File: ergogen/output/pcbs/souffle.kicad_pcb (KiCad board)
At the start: 2 copper layers, 130.3 x 93.2 mm, 162 parts

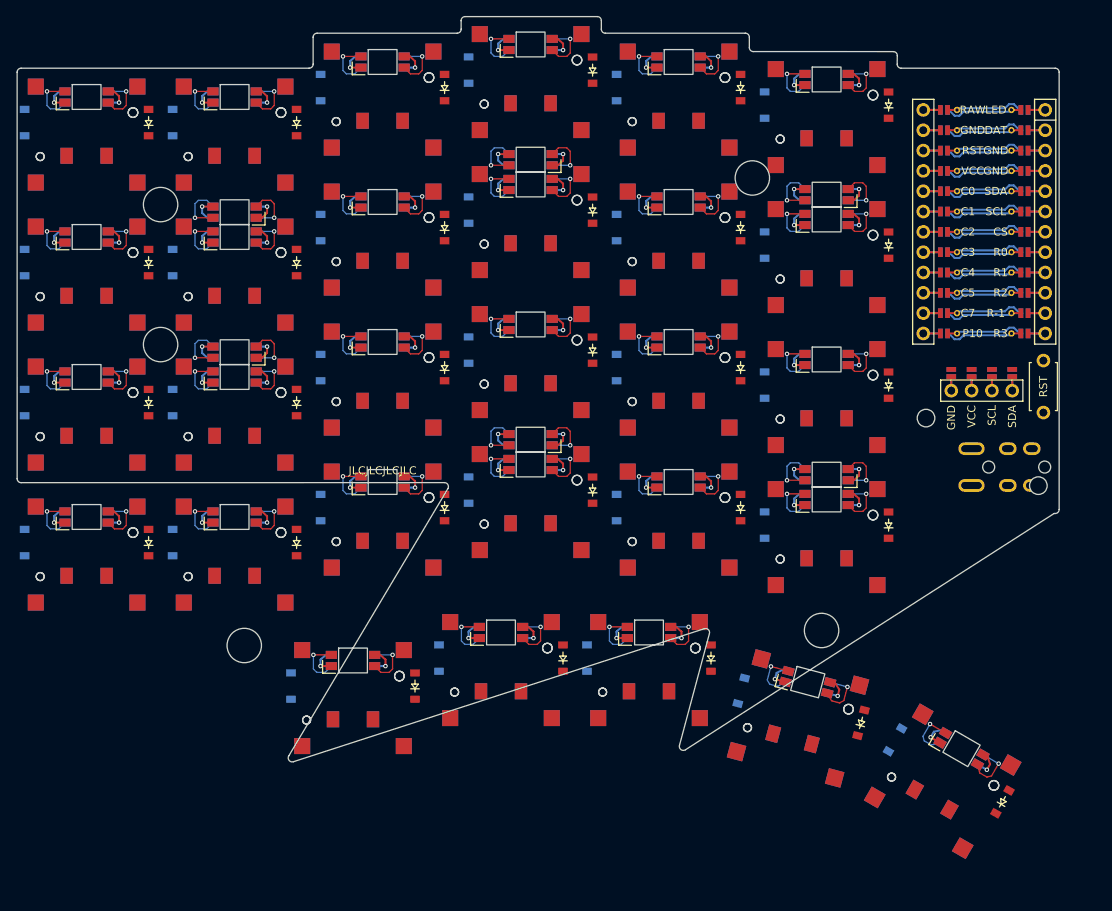
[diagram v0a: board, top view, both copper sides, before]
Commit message: fix: number row on top and improved outline
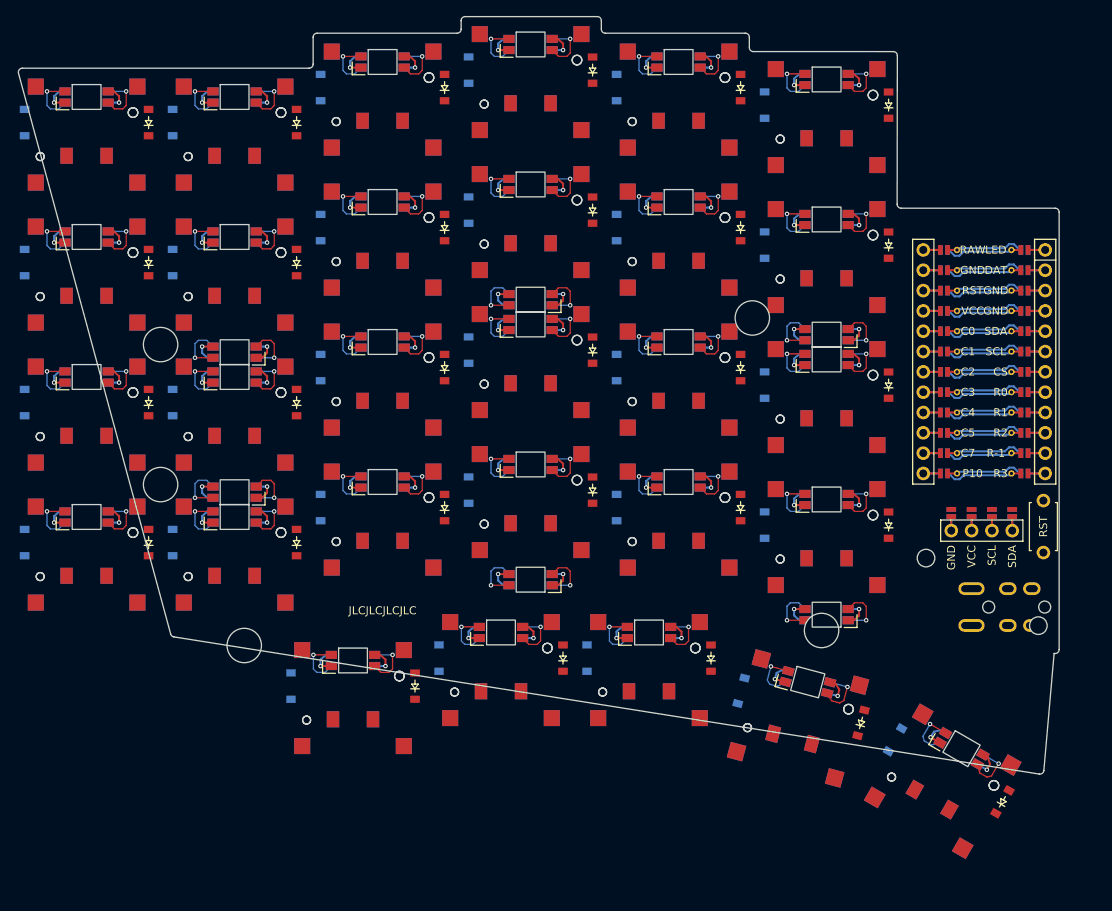
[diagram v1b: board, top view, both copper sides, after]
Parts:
- moved MCU1 17.5 mm to (212.2, 74.6)
- moved MH5 17.5 mm to (183.2, 70.4)
- moved LED30 17.5 mm to (192.5, 72.5)
- moved LED31 17.5 mm to (155.5, 68.1)
- moved LED32 17.5 mm to (118.5, 74.7)
- moved LED33 17.5 mm to (118.5, 92.2)
- moved LED34 17.5 mm to (155.5, 103.1)
- moved LED35 17.5 mm to (192.5, 107.5)
- moved MH1 17.5 mm to (204.9, 100.4)
- moved MH2 17.5 mm to (219.0, 108.9)
- moved MH3 17.5 mm to (109.2, 73.8)
- moved MH4 17.5 mm to (109.2, 91.2)
- moved RST1 17.5 mm to (219.6, 96.5)
- moved TRRS1 17.5 mm to (221.4, 106.6)
- moved DISP1 17.5 mm to (211.9, 80.3)
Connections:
- D1 pad 1: R-1 -> R2
- D1 pad 2: outer_number_B -> outer_bottom_B
- D10 pad 1: R2 -> R1
- D10 pad 2: ring_bottom_B -> ring_home_B
- D11 pad 1: R1 -> R0
- D11 pad 2: ring_home_B -> ring_top_B
- D12 pad 1: R0 -> R4
- D12 pad 2: ring_top_B -> ring_number_B
- D13 pad 1: R-1 -> R2
- D13 pad 2: middle_number_B -> middle_bottom_B
- D14 pad 1: R2 -> R1
- D14 pad 2: middle_bottom_B -> middle_home_B
- D15 pad 1: R1 -> R0
- D15 pad 2: middle_home_B -> middle_top_B
- D16 pad 1: R0 -> R4
- D16 pad 2: middle_top_B -> middle_number_B
- D17 pad 1: R-1 -> R2
- D17 pad 2: index_number_B -> index_bottom_B
- D18 pad 1: R2 -> R1
- D18 pad 2: index_bottom_B -> index_home_B
- D19 pad 1: R1 -> R0
- D19 pad 2: index_home_B -> index_top_B
- D2 pad 1: R2 -> R1
- D2 pad 2: outer_bottom_B -> outer_home_B
- D20 pad 1: R0 -> R4
- D20 pad 2: index_top_B -> index_number_B
- D21 pad 1: R-1 -> R2
- D21 pad 2: inner_number_B -> inner_bottom_B
- D22 pad 1: R2 -> R1
- D22 pad 2: inner_bottom_B -> inner_home_B
- D23 pad 1: R1 -> R0
- D23 pad 2: inner_home_B -> inner_top_B
- D24 pad 1: R0 -> R4
- D24 pad 2: inner_top_B -> inner_number_B
- D3 pad 1: R1 -> R0
- D3 pad 2: outer_home_B -> outer_top_B
- D30 pad 1: R-1 -> R2
- D30 pad 2: outer_number_F -> outer_bottom_F
- D31 pad 1: R2 -> R1
- D31 pad 2: outer_bottom_F -> outer_home_F
- D32 pad 1: R1 -> R0
- D32 pad 2: outer_home_F -> outer_top_F
- D33 pad 1: R0 -> R4
- D33 pad 2: outer_top_F -> outer_number_F
- D34 pad 1: R-1 -> R2
- D34 pad 2: pinky_number_F -> pinky_bottom_F
- D35 pad 1: R2 -> R1
- D35 pad 2: pinky_bottom_F -> pinky_home_F
- D36 pad 1: R1 -> R0
- D36 pad 2: pinky_home_F -> pinky_top_F
- D37 pad 1: R0 -> R4
- D37 pad 2: pinky_top_F -> pinky_number_F
- D38 pad 1: R-1 -> R2
- D38 pad 2: ring_number_F -> ring_bottom_F
- D39 pad 1: R2 -> R1
- D39 pad 2: ring_bottom_F -> ring_home_F
- D4 pad 1: R0 -> R4
- D4 pad 2: outer_top_B -> outer_number_B
- D40 pad 1: R1 -> R0
- D40 pad 2: ring_home_F -> ring_top_F
- D41 pad 1: R0 -> R4
- D41 pad 2: ring_top_F -> ring_number_F
- D42 pad 1: R-1 -> R2
- D42 pad 2: middle_number_F -> middle_bottom_F
- D43 pad 1: R2 -> R1
- D43 pad 2: middle_bottom_F -> middle_home_F
- D44 pad 1: R1 -> R0
- D44 pad 2: middle_home_F -> middle_top_F
- D45 pad 1: R0 -> R4
- D45 pad 2: middle_top_F -> middle_number_F
- D46 pad 1: R-1 -> R2
- D46 pad 2: index_number_F -> index_bottom_F
- D47 pad 1: R2 -> R1
- D47 pad 2: index_bottom_F -> index_home_F
- D48 pad 1: R1 -> R0
- D48 pad 2: index_home_F -> index_top_F
- D49 pad 1: R0 -> R4
- D49 pad 2: index_top_F -> index_number_F
- D5 pad 1: R-1 -> R2
- D5 pad 2: pinky_number_B -> pinky_bottom_B
- D50 pad 1: R-1 -> R2
- D50 pad 2: inner_number_F -> inner_bottom_F
- D51 pad 1: R2 -> R1
- D51 pad 2: inner_bottom_F -> inner_home_F
- D52 pad 1: R1 -> R0
- D52 pad 2: inner_home_F -> inner_top_F
- D53 pad 1: R0 -> R4
- D53 pad 2: inner_top_F -> inner_number_F
- D6 pad 1: R2 -> R1
- D6 pad 2: pinky_bottom_B -> pinky_home_B
- D7 pad 1: R1 -> R0
- D7 pad 2: pinky_home_B -> pinky_top_B
- D8 pad 1: R0 -> R4
- D8 pad 2: pinky_top_B -> pinky_number_B
- D9 pad 1: R-1 -> R2
- D9 pad 2: ring_number_B -> ring_bottom_B
- LED1 pad 2: LED_18 -> LED_21
- LED1 pad 4: LED_19 -> LED_20
- LED10 pad 2: LED_15 -> LED_14
- LED10 pad 4: LED_14 -> LED_13
- LED11 pad 2: LED_14 -> LED_13
- LED11 pad 4: LED_13 -> LED_12
- LED12 pad 2: LED_13 -> LED_12
- LED12 pad 4: LED_12 -> LED_13
- LED13 pad 2: LED_11 -> LED_10
- LED13 pad 4: LED_12 -> LED_9
- LED14 pad 2: LED_10 -> LED_11
- LED14 pad 4: LED_9 -> LED_10
- LED15 pad 2: LED_11 -> LED_12
- LED15 pad 4: LED_10 -> LED_11
- LED16 pad 2: LED_12 -> LED_11
- LED16 pad 4: LED_11 -> LED_12
- LED17 pad 2: LED_4 -> LED_7
- LED17 pad 4: LED_5 -> LED_6
- LED18 pad 2: LED_7 -> LED_6
- LED18 pad 4: LED_6 -> LED_5
- LED19 pad 2: LED_6 -> LED_5
- LED19 pad 4: LED_5 -> LED_4
- LED2 pad 2: LED_21 -> LED_20
- LED2 pad 4: LED_20 -> LED_19
- LED20 pad 2: LED_5 -> LED_4
- LED20 pad 4: LED_4 -> LED_5
- LED21 pad 2: LED_3 -> LED_2
- LED21 pad 4: LED_4 -> LED_1
- LED22 pad 2: LED_2 -> LED_3
- LED22 pad 4: LED_1 -> LED_2
- LED23 pad 2: LED_3 -> LED_4
- LED23 pad 4: LED_2 -> LED_3
- LED24 pad 2: LED_4 -> LED_3
- LED24 pad 4: LED_3 -> LED_4
- LED3 pad 2: LED_20 -> LED_19
- LED3 pad 4: LED_19 -> LED_18
- LED4 pad 2: LED_19 -> LED_18
- LED4 pad 4: LED_18 -> LED_19
- LED5 pad 2: LED_17 -> LED_16
- LED5 pad 4: LED_16 -> LED_15
- LED6 pad 2: LED_16 -> LED_17
- LED6 pad 4: LED_15 -> LED_16
- LED7 pad 2: LED_17 -> LED_18
- LED7 pad 4: LED_16 -> LED_17
- LED8 pad 2: LED_18 -> LED_17
- LED8 pad 4: LED_17 -> LED_16
- LED9 pad 2: LED_12 -> LED_15
- LED9 pad 4: LED_13 -> LED_14
- S1 pad 1: outer_number_B -> outer_bottom_B
- S10 pad 1: ring_bottom_B -> ring_home_B
- S11 pad 1: ring_home_B -> ring_top_B
- S12 pad 1: ring_top_B -> ring_number_B
- S13 pad 1: middle_number_B -> middle_bottom_B
- S14 pad 1: middle_bottom_B -> middle_home_B
- S15 pad 1: middle_home_B -> middle_top_B
- S16 pad 1: middle_top_B -> middle_number_B
- S17 pad 1: index_number_B -> index_bottom_B
- S18 pad 1: index_bottom_B -> index_home_B
- S19 pad 1: index_home_B -> index_top_B
- S2 pad 1: outer_bottom_B -> outer_home_B
- S20 pad 1: index_top_B -> index_number_B
- S21 pad 1: inner_number_B -> inner_bottom_B
- S22 pad 1: inner_bottom_B -> inner_home_B
- S23 pad 1: inner_home_B -> inner_top_B
- S24 pad 1: inner_top_B -> inner_number_B
- S3 pad 1: outer_home_B -> outer_top_B
- S30 pad 1: outer_number_F -> outer_bottom_F
- S31 pad 1: outer_bottom_F -> outer_home_F
- S32 pad 1: outer_home_F -> outer_top_F
- S33 pad 1: outer_top_F -> outer_number_F
- S34 pad 1: pinky_number_F -> pinky_bottom_F
- S35 pad 1: pinky_bottom_F -> pinky_home_F
- S36 pad 1: pinky_home_F -> pinky_top_F
- S37 pad 1: pinky_top_F -> pinky_number_F
- S38 pad 1: ring_number_F -> ring_bottom_F
- S39 pad 1: ring_bottom_F -> ring_home_F
- S4 pad 1: outer_top_B -> outer_number_B
- S40 pad 1: ring_home_F -> ring_top_F
- S41 pad 1: ring_top_F -> ring_number_F
- S42 pad 1: middle_number_F -> middle_bottom_F
- S43 pad 1: middle_bottom_F -> middle_home_F
- S44 pad 1: middle_home_F -> middle_top_F
- S45 pad 1: middle_top_F -> middle_number_F
- S46 pad 1: index_number_F -> index_bottom_F
- S47 pad 1: index_bottom_F -> index_home_F
- S48 pad 1: index_home_F -> index_top_F
- S49 pad 1: index_top_F -> index_number_F
- S5 pad 1: pinky_number_B -> pinky_bottom_B
- S50 pad 1: inner_number_F -> inner_bottom_F
- S51 pad 1: inner_bottom_F -> inner_home_F
- S52 pad 1: inner_home_F -> inner_top_F
- S53 pad 1: inner_top_F -> inner_number_F
- S6 pad 1: pinky_bottom_B -> pinky_home_B
- S7 pad 1: pinky_home_B -> pinky_top_B
- S8 pad 1: pinky_top_B -> pinky_number_B
- S9 pad 1: ring_number_B -> ring_bottom_B
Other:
- board size 130.3 x 93.2 mm -> 130.1 x 94.7 mm

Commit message: feat: outline improvements
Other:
- board size 130.1 x 94.7 mm -> 134.9 x 109.8 mm
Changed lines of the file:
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@@
   (segment (start 197.45 106.4525) (end 197.45 108.2125) (width 0.15) (layer "F.Cu") (net 143))
   (segment (start 197.029 106.0275) (end 197.45 106.4525) (width 0.15) (layer "F.Cu") (net 143))
-  (gr_line (start 110.50826649856596 109.92527651860325) (end 91.48622889852672 39.83343914341975) (layer Edge.Cuts) (stroke (width 0.15) (type default)))
-(gr_line (start 91.9687610950968 39.202482330781216) (end 127.8150135 39.201513513148655) (layer Edge.Cuts) (stroke (width 0.15) (type default)))
+  (gr_line (start 91.2502786953727 111.93679999635788) (end 91.31455549192064 39.702041598866344) (layer Edge.Cuts) (stroke (width 0.15) (type default)))
+(gr_line (start 91.81454179192065 39.202486498870485) (end 127.8150135 39.20151351314865) (layer Edge.Cuts) (stroke (width 0.15) (type default)))
 (gr_line (start 128.315 38.701513513148655) (end 128.315 35.3275) (layer Edge.Cuts) (stroke (width 0.15) (type default)))
 (gr_line (start 128.815 34.8275) (end 146.315 34.8275) (layer Edge.Cuts) (stroke (width 0.15) (type default)))
@@
 (gr_line (start 183.34287840000002 37.12312159204324) (end 200.8424827703032 37.12737825256575) (layer Edge.Cuts) (stroke (width 0.15) (type default)))
 (gr_line (start 201.34236077036712 37.628016802540515) (end 201.31863938512134 56.201861450012075) (layer Edge.Cuts) (stroke (width 0.15) (type default)))
-(gr_line (start 220.93800000000002 112.3635) (end 219.65752596395185 126.98539423067496) (layer Edge.Cuts) (stroke (width 0.15) (type default)))
-(gr_line (start 219.08114720800037 127.43560839237159) (end 110.91252714391037 110.28815311369672) (layer Edge.Cuts) (stroke (width 0.15) (type default)))
+(gr_line (start 221.6070711821377 104.9663415844974) (end 226.0923281969262 115.6359149762103) (layer Edge.Cuts) (stroke (width 0.15) (type default)))
+(gr_line (start 226.0654764006069 116.07782689603465) (end 211.09156059668345 142.27125340028437) (layer Edge.Cuts) (stroke (width 0.15) (type default)))
+(gr_line (start 210.44136417514045 142.47398553796899) (end 176.60167485384602 126.25365946744344) (layer Edge.Cuts) (stroke (width 0.15) (type default)))
+(gr_line (start 176.4280428580794 126.20634746780448) (end 161.62301991140092 124.94372737349019) (layer Edge.Cuts) (stroke (width 0.15) (type default)))
+(gr_line (start 161.4782637171782 124.95248967103738) (end 144.8505883399894 128.42692930209176) (layer Edge.Cuts) (stroke (width 0.15) (type default)))
+(gr_line (start 144.74831955000005 128.4375) (end 124.6650889942857 128.4375) (layer Edge.Cuts) (stroke (width 0.15) (type default)))
+(gr_line (start 124.44649265438869 128.38718392921672) (end 91.53168215547566 112.38692882557845) (layer Edge.Cuts) (stroke (width 0.15) (type default)))
 (gr_line (start 201.81863898518517 56.7025) (end 221.068 56.7025) (layer Edge.Cuts) (stroke (width 0.15) (type default)))
-(gr_line (start 221.568 57.2025) (end 221.568 111.8635) (layer Edge.Cuts) (stroke (width 0.15) (type default)))
-(gr_line (start 221.068 112.3635) (end 220.93800000000002 112.3635) (layer Edge.Cuts) (stroke (width 0.15) (type default)))
-(gr_arc (start 91.9687610950968 39.20248233078121) (mid 91.5716065950968 39.39874303078121) (end 91.48622889509679 39.83343913078121) (layer Edge.Cuts) (stroke (width 0.15) (type default)))
+(gr_line (start 221.568 57.2025) (end 221.568 104.77257712698844) (layer Edge.Cuts) (stroke (width 0.15) (type default)))
+(gr_arc (start 91.81454179192065 39.202486498863436) (mid 91.46115449192064 39.348780598863435) (end 91.31455549192064 39.70204159886344) (layer Edge.Cuts) (stroke (width 0.15) (type default)))
 (gr_arc (start 127.81501349999999 39.201513513148655) (mid 128.1685582 39.05506211314866) (end 128.315 38.701513513148655) (layer Edge.Cuts) (stroke (width 0.15) (type default)))
 (gr_arc (start 128.815 34.8275) (mid 128.4614466 34.9739466) (end 128.315 35.3275) (layer Edge.Cuts) (stroke (width 0.15) (type default)))
@@
 (gr_arc (start 201.31863938518518 56.20186150001397) (mid 201.46485988518518 56.55582760001397) (end 201.81863908518517 56.70250000001397) (layer Edge.Cuts) (stroke (width 0.15) (type default)))
 (gr_arc (start 221.568 57.2025) (mid 221.42155340000002 56.8489466) (end 221.068 56.7025) (layer Edge.Cuts) (stroke (width 0.15) (type default)))
-(gr_arc (start 221.068 112.3635) (mid 221.42155340000002 112.2170534) (end 221.568 111.8635) (layer Edge.Cuts) (stroke (width 0.15) (type default)))
-(gr_arc (start 219.08114715922605 127.43560838463978) (mid 219.46721955922604 127.33581428463978) (end 219.65752595922604 126.98539428463978) (layer Edge.Cuts) (stroke (width 0.15) (type default)))
-(gr_arc (start 110.50826649513606 109.92527650596477) (mid 110.65681719513606 110.16640490596477) (end 110.91252709513606 110.28815320596476) (layer Edge.Cuts) (stroke (width 0.15) (type default)))
+(gr_arc (start 221.568 104.77257712698844) (mid 221.57786510000003 104.87140932698844) (end 221.6070712 104.96634152698844) (layer Edge.Cuts) (stroke (width 0.15) (type default)))
+(gr_arc (start 226.0654763790639 116.07782693371927) (mid 226.1304788790639 115.86000493371927) (end 226.0923281790639 115.63591503371926) (layer Edge.Cuts) (stroke (width 0.15) (type default)))
+(gr_arc (start 210.44136417514042 142.47398553796899) (mid 210.80631727514043 142.50044073796897) (end 211.09156057514042 142.27125343796897) (layer Edge.Cuts) (stroke (width 0.15) (type default)))
+(gr_arc (start 176.60167485384602 126.25365946744346) (mid 176.51700495384603 126.22212736744345) (end 176.42804285384602 126.20634746744345) (layer Edge.Cuts) (stroke (width 0.15) (type default)))
+(gr_arc (start 161.62301990716756 124.94372737312915) (mid 161.55032240716756 124.94283237312915) (end 161.47826370716757 124.95248957312914) (layer Edge.Cuts) (stroke (width 0.15) (type default)))
+(gr_arc (start 144.74831955000005 128.4375) (mid 144.79972635000004 128.4348503) (end 144.85058835000004 128.4269294) (layer Edge.Cuts) (stroke (width 0.15) (type default)))
+(gr_arc (start 124.4464926942857 128.3871839) (mid 124.5529327942857 128.4247586) (end 124.6650889942857 128.4375) (layer Edge.Cuts) (stroke (width 0.15) (type default)))
+(gr_arc (start 91.25027869537269 111.93679999636173) (mid 91.32631019537268 112.20229379636173) (end 91.53168219537268 112.38692879636173) (layer Edge.Cuts) (stroke (width 0.15) (type default)))
 )

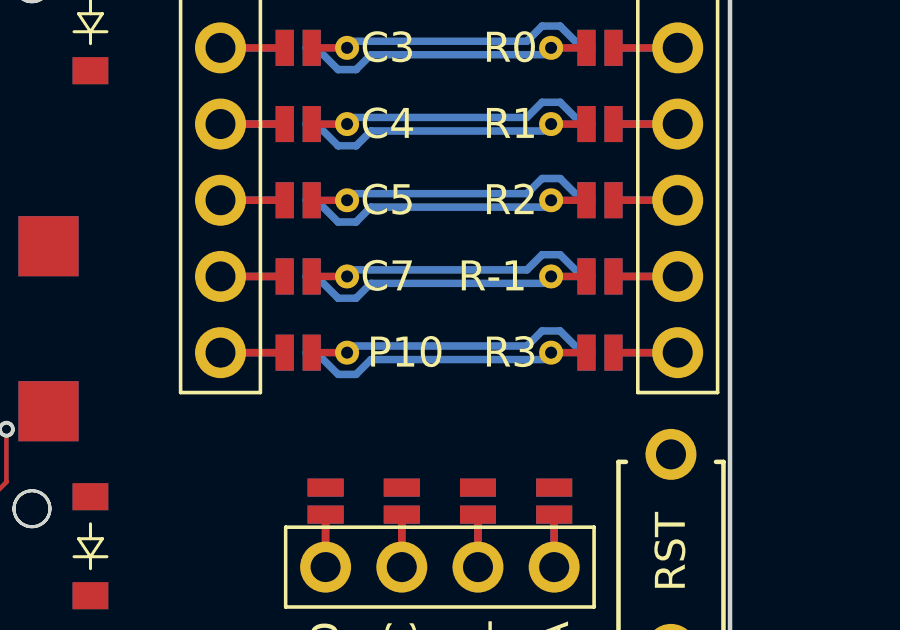
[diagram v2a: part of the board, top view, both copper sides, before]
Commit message: feat: LED and switches ratsnest
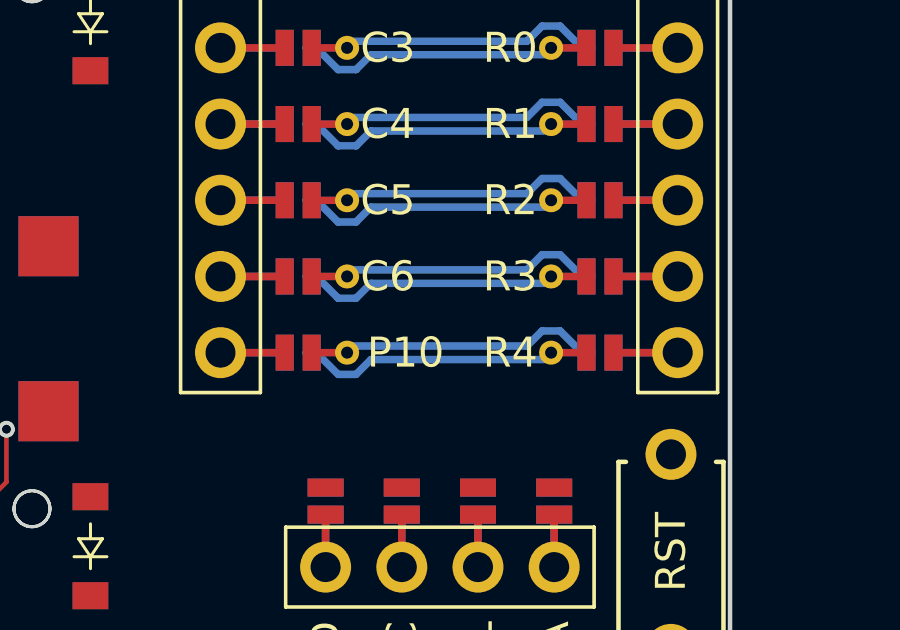
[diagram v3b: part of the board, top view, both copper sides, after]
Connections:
- D1 pad 1: R2 -> R3
- D10 pad 1: R1 -> R2
- D11 pad 1: R0 -> R1
- D12 pad 1: R4 -> R0
- D13 pad 1: R2 -> R3
- D14 pad 1: R1 -> R2
- D15 pad 1: R0 -> R1
- D16 pad 1: R4 -> R0
- D17 pad 1: R2 -> R3
- D18 pad 1: R1 -> R2
- D19 pad 1: R0 -> R1
- D2 pad 1: R1 -> R2
- D20 pad 1: R4 -> R0
- D21 pad 1: R2 -> R3
- D22 pad 1: R1 -> R2
- D23 pad 1: R0 -> R1
- D24 pad 1: R4 -> R0
- D25 pad 1: R3 -> R4
- D26 pad 1: R3 -> R4
- D27 pad 1: R3 -> R4
- D28 pad 1: R3 -> R4
- D29 pad 1: R3 -> R4
- D3 pad 1: R0 -> R1
- D30 pad 1: R2 -> R3
- D31 pad 1: R1 -> R2
- D32 pad 1: R0 -> R1
- D33 pad 1: R4 -> R0
- D34 pad 1: R2 -> R3
- D35 pad 1: R1 -> R2
- D36 pad 1: R0 -> R1
- D37 pad 1: R4 -> R0
- D38 pad 1: R2 -> R3
- D39 pad 1: R1 -> R2
- D4 pad 1: R4 -> R0
- D40 pad 1: R0 -> R1
- D41 pad 1: R4 -> R0
- D42 pad 1: R2 -> R3
- D43 pad 1: R1 -> R2
- D44 pad 1: R0 -> R1
- D45 pad 1: R4 -> R0
- D46 pad 1: R2 -> R3
- D47 pad 1: R1 -> R2
- D48 pad 1: R0 -> R1
- D49 pad 1: R4 -> R0
- D5 pad 1: R2 -> R3
- D50 pad 1: R2 -> R3
- D51 pad 1: R1 -> R2
- D52 pad 1: R0 -> R1
- D53 pad 1: R4 -> R0
- D54 pad 1: R3 -> R4
- D55 pad 1: R3 -> R4
- D56 pad 1: R3 -> R4
- D57 pad 1: R3 -> R4
- D58 pad 1: R3 -> R4
- D6 pad 1: R1 -> R2
- D7 pad 1: R0 -> R1
- D8 pad 1: R4 -> R0
- D9 pad 1: R2 -> R3
- LED1 pad 2: LED_21 -> LED_27
- LED1 pad 4: LED_20 -> LED_26
- LED10 pad 2: LED_14 -> LED_17
- LED10 pad 4: LED_13 -> LED_16
- LED11 pad 2: LED_13 -> LED_16
- LED11 pad 4: LED_12 -> LED_15
- LED12 pad 2: LED_12 -> LED_15
- LED12 pad 4: LED_13 -> LED_14
- LED13 pad 2: LED_10 -> LED_11
- LED13 pad 4: LED_9 -> LED_10
- LED14 pad 2: LED_11 -> LED_12
- LED14 pad 4: LED_10 -> LED_11
- LED15 pad 2: LED_12 -> LED_13
- LED15 pad 4: LED_11 -> LED_12
- LED16 pad 2: LED_11 -> LED_14
- LED16 pad 4: LED_12 -> LED_13
- LED17 pad 2: LED_7 -> LED_10
- LED17 pad 4: LED_6 -> LED_9
- LED18 pad 2: LED_6 -> LED_8
- LED18 pad 4: LED_5 -> LED_7
- LED19 pad 2: LED_5 -> LED_7
- LED19 pad 4: LED_4 -> LED_6
- LED2 pad 2: LED_20 -> LED_26
- LED2 pad 4: LED_19 -> LED_25
- LED20 pad 2: LED_4 -> LED_6
- LED24 pad 2: LED_3 -> LED_5
- LED25 pad 2: LED_22 -> LED_28
- LED25 pad 4: LED_21 -> LED_27
- LED26 pad 2: LED_23 -> LED_29
- LED26 pad 4: LED_22 -> LED_28
- LED27 pad 2: LED_24 -> LED_31
- LED27 pad 4: LED_23 -> LED_30
- LED28 pad 2: LED_25 -> LED_32
- LED28 pad 4: LED_24 -> LED_31
- LED29 pad 2: LED_24 -> LED_33
- LED29 pad 4: LED_25 -> LED_32
- LED3 pad 2: LED_19 -> LED_25
- LED3 pad 4: LED_18 -> LED_24
- LED4 pad 2: LED_18 -> LED_24
- LED4 pad 4: LED_19 -> LED_23
- LED5 pad 2: LED_16 -> LED_19
- LED5 pad 4: LED_15 -> LED_18
- LED6 pad 2: LED_17 -> LED_20
- LED6 pad 4: LED_16 -> LED_21
- LED7 pad 2: LED_18 -> LED_21
- LED7 pad 4: LED_17 -> LED_22
- LED8 pad 2: LED_17 -> LED_22
- LED8 pad 4: LED_16 -> LED_23
- LED9 pad 2: LED_15 -> LED_18
- LED9 pad 4: LED_14 -> LED_17
- MCU1 pad 111: R-1 -> R3
- MCU1 pad 112: R3 -> R4
- MCU1 pad 114: C7 -> C6
- S25 pad 2: C6 -> C1
- S26 pad 2: C7 -> C2
- S27 pad 2: C8 -> C3
- S28 pad 2: C9 -> C4
- S29 pad 2: C10 -> C5
- S54 pad 2: C6 -> C1
- S55 pad 2: C7 -> C2
- S56 pad 2: C8 -> C3
- S57 pad 2: C9 -> C4
- S58 pad 2: C10 -> C5
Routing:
- net LED_4: track 27.1 -> 13.5 mm, vias 4 -> 2
- net LED_28: track 0.00 -> 13.5 mm, vias 0 -> 2
- net LED_27: track 0.00 -> 13.5 mm, vias 0 -> 2
- net LED_26: track 0.00 -> 13.5 mm, vias 0 -> 2
- net LED_19: track 20.3 -> 6.76 mm, vias 3 -> 1
- net LED_12: track 27.1 -> 13.5 mm, vias 4 -> 2
- net LED_31: track 0.00 -> 13.5 mm, vias 0 -> 2
- net LED_32: track 0.00 -> 13.5 mm, vias 0 -> 2
- net LED_8: track 0.00 -> 6.76 mm, vias 0 -> 1
- net LED_7: track 6.76 -> 13.5 mm, vias 1 -> 2
- net LED_30: track 0.00 -> 6.76 mm, vias 0 -> 1
- net LED_29: track 0.00 -> 6.76 mm, vias 0 -> 1
- net LED_20: track 13.5 -> 6.76 mm, vias 2 -> 1
- net LED_18: track 20.3 -> 13.5 mm, vias 3 -> 2
- net LED_17: track 20.3 -> 13.5 mm, vias 3 -> 2
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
